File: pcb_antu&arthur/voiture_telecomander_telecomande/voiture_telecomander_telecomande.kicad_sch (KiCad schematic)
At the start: 31 parts, among them J1 batterie, J2 Ecran 7 segments, J3 bouton1, J4 bouton2, J5 interrupteur, J6 RGB, U1 ESP32-C6-DEVKITC-1-N8, U2 COM-09032

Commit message: changement de +5v à Alim_ESP
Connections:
- net +5V renamed Alim_ESP
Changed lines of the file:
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@@
+		)
+	)
+	(label "Alim_ESP"
+		(at 96.52 114.3 0)
+		(effects
+			(font
+				(size 1.27 1.27)
+			)
+			(justify left bottom)
 		)
 	)
@@
 		)
 	)
+	(label "Alim_ESP"
+		(at 55.88 114.3 180)
+		(effects
+			(font
+				(size 1.27 1.27)
+			)
+			(justify right bottom)
+		)
+	)
 	(label "DIO_ECRAN"
 		(at 55.88 88.9 180)
@@
 		)
 	)
+	(label "Alim_ESP"
+		(at 238.76 138.43 180)
+		(effects
+			(font
+				(size 1.27 1.27)
+			)
+			(justify right bottom)
+		)
+	)
 	(label "G"
 		(at 77.47 175.26 180)
@@
 	)
 	(symbol
-		(lib_id "power:+5V")
-		(at 238.76 138.43 90)
-		(unit 1)
-		(exclude_from_sim no)
-		(in_bom yes)
-		(on_board yes)
-		(dnp no)
-		(fields_autoplaced yes)
-		(property "Reference" "#PWR03"
-			(at 242.57 138.43 0)
-			(effects
-				(font
-					(size 1.27 1.27)
-				)
-				(hide yes)
-			)
-		)
-		(property "Value" "+5V"
-			(at 234.95 138.4299 90)
-			(effects
-				(font
-					(size 1.27 1.27)
-				)
-				(justify left)
-			)
-		)
-		(property "Footprint" ""
-			(at 238.76 138.43 0)
-			(effects
-				(font
-					(size 1.27 1.27)
-				)
-				(hide yes)
-			)
-		)
-		(property "Datasheet" ""
-			(at 238.76 138.43 0)
-			(effects
-				(font
-					(size 1.27 1.27)
-				)
-				(hide yes)
-			)
-		)
-		(property "Description" "Power symbol creates a global label with name \"+5V\""
-			(at 238.76 138.43 0)
-			(effects
-				(font
-					(size 1.27 1.27)
-				)
-				(hide yes)
-			)
-		)
-		(pin "1"
-		)
-		(instances
-			(project ""
-				(path "/570fb641-a88b-4e77-9989-d06242766e90"
-					(reference "#PWR03")
-					(unit 1)
-				)
-			)
-		)
-	)
-	(symbol
-		(lib_id "power:+5V")
-		(at 96.52 114.3 270)
-		(unit 1)
-		(exclude_from_sim no)
-		(in_bom yes)
-		(on_board yes)
-		(dnp no)
-		(fields_autoplaced yes)
-		(property "Reference" "#PWR09"
-			(at 92.71 114.3 0)
-			(effects
-				(font
-					(size 1.27 1.27)
-				)
-				(hide yes)
-			)
-		)
-		(property "Value" "+5V"
-			(at 100.33 114.2999 90)
-			(effects
-				(font
-					(size 1.27 1.27)
-				)
-				(justify left)
-			)
-		)
-		(property "Footprint" ""
-			(at 96.52 114.3 0)
-			(effects
-				(font
-					(size 1.27 1.27)
-				)
-				(hide yes)
-			)
-		)
-		(property "Datasheet" ""
-			(at 96.52 114.3 0)
-			(effects
-				(font
-					(size 1.27 1.27)
-				)
-				(hide yes)
-			)
-		)
-		(property "Description" "Power symbol creates a global label with name \"+5V\""
-			(at 96.52 114.3 0)
-			(effects
-				(font
-					(size 1.27 1.27)
-				)
-				(hide yes)
-			)
-		)
-		(pin "1"
-		)
-		(instances
-			(project ""
-				(path "/570fb641-a88b-4e77-9989-d06242766e90"
-					(reference "#PWR09")
-					(unit 1)
-				)
-			)
-		)
-	)
-	(symbol
 		(lib_id "power:GND")
 		(at 190.5 104.14 270)
@@
 					(unit 1)
 				)
-			)
-		)
-	)
-	(symbol
-		(lib_id "power:+5V")
-		(at 55.88 114.3 90)
-		(unit 1)
-		(exclude_from_sim no)
-		(in_bom yes)
-		(on_board yes)
-		(dnp no)
-		(fields_autoplaced yes)
-		(property "Reference" "#PWR08"
-			(at 59.69 114.3 0)
-			(effects
-				(font
-					(size 1.27 1.27)
-				)
-				(hide yes)
-			)
-		)
-		(property "Value" "+5V"
-			(at 52.07 114.2999 90)
-			(effects
-				(font
-					(size 1.27 1.27)
-				)
-				(justify left)
-			)
-		)
-		(property "Footprint" ""
-			(at 55.88 114.3 0)
-			(effects
-				(font
-					(size 1.27 1.27)
-				)
-				(hide yes)
-			)
-		)
-		(property "Datasheet" ""
-			(at 55.88 114.3 0)
-			(effects
-				(font
-					(size 1.27 1.27)
-				)
-				(hide yes)
-			)
-		)
-		(property "Description" "Power symbol creates a global label with name \"+5V\""
-			(at 55.88 114.3 0)
-			(effects
-				(font
-					(size 1.27 1.27)
-				)
-				(hide yes)
-			)
-		)
-		(pin "1"
-		)
-		(instances
-			(project ""
-				(path "/570fb641-a88b-4e77-9989-d06242766e90"
-					(reference "#PWR08")
-					(unit 1)
-				)

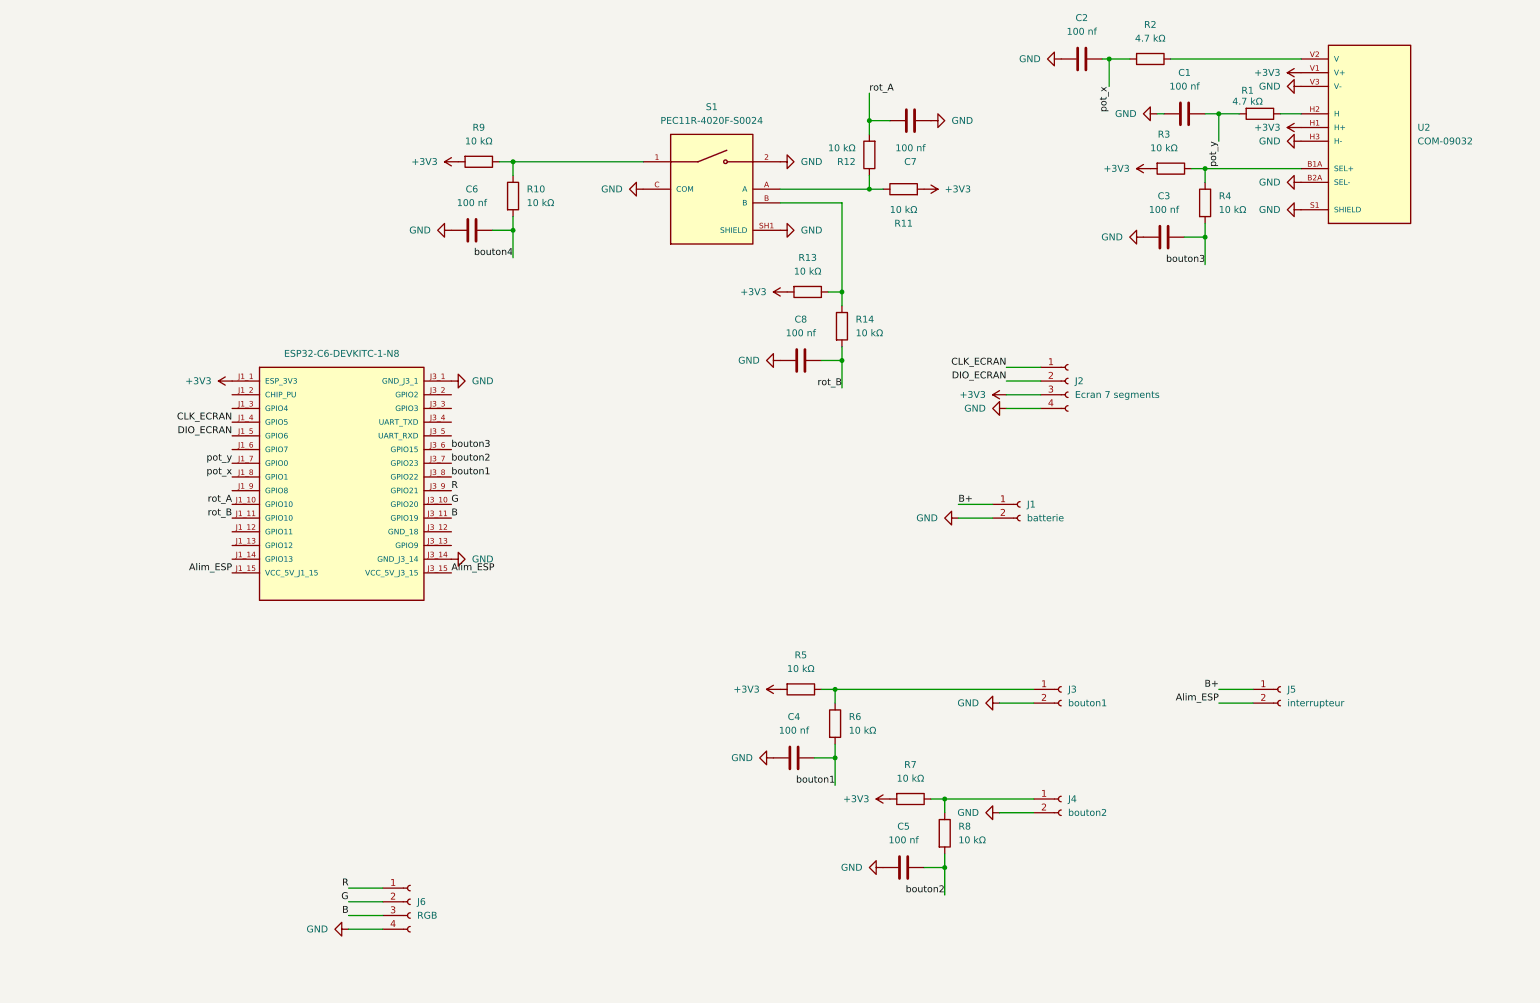
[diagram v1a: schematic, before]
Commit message: changement purement estetique dans le schema pour une meileur compréhension
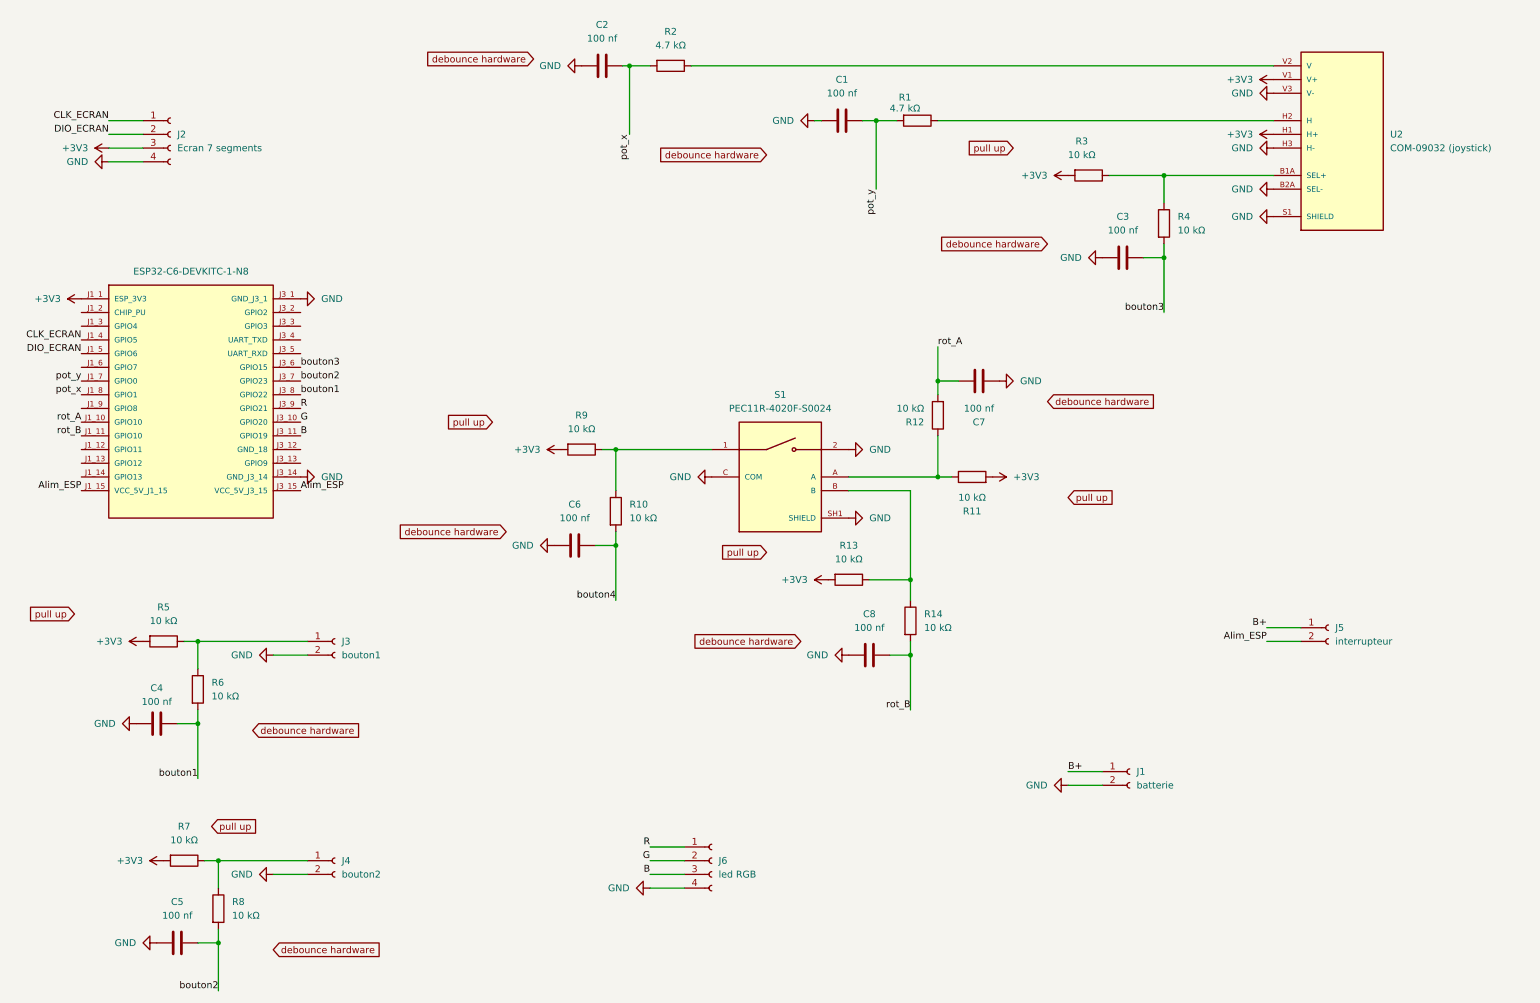
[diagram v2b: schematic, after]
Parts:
- J6: value RGB -> led RGB
- U2: value COM-09032 -> COM-09032 (joystick)
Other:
- moved on the sheet: C1, C2, C3, C4, C5, C6, C7, C8, J1, J2, J3, J4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

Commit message: mise a jour PCB antu_arthur
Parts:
- added J7: Conn_01x06_Socket, Connector_PinSocket_2.54mm:PinSocket_1x06_P2.54mm_Vertical, symbol Connector:Conn_01x06_Socket
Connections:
- net +3V3: now also J6.4 (Pin_4)
- net Alim_ESP: no longer J5.2 (Pin_2)
- net GND: now also J7.3 (Pin_3), J7.4 (Pin_4); no longer J6.4 (Pin_4)
- new net +5V: J7.5 (Pin_5), J7.6 (Pin_6)
- new net +BATT: J5.2 (Pin_2), J7.1 (Pin_1), J7.2 (Pin_2)

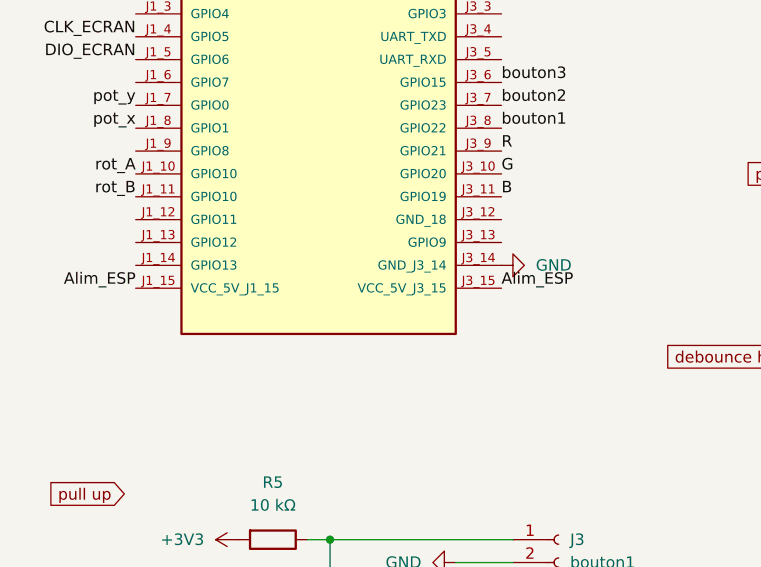
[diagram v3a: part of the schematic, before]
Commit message: ajout d'un converter buck
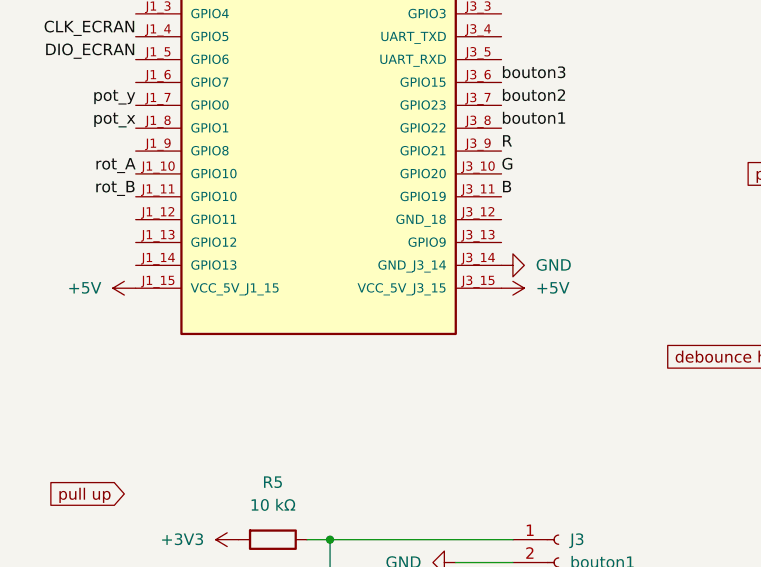
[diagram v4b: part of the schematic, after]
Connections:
- net Alim_ESP is gone; now on net +5V: U1.J1_15 (VCC_5V_J1_15), U1.J3_15 (VCC_5V_J3_15)
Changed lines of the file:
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@@
-		)
-	)
-	(label "Alim_ESP"
-		(at 68.58 99.06 0)
-		(effects
-			(font
-				(size 1.27 1.27)
-			)
-			(justify left bottom)
 		)
 	)
 	(label "R"
 		(at 133.35 165.1 180)
-		(effects
-			(font
-				(size 1.27 1.27)
-			)
-			(justify right bottom)
-		)
-	)
-	(label "Alim_ESP"
-		(at 27.94 99.06 180)
 		(effects
 			(font
@@
 	)
 	(symbol
+		(lib_id "power:+5V")
+		(at 68.58 99.06 270)
+		(unit 1)
+		(exclude_from_sim no)
+		(in_bom yes)
+		(on_board yes)
+		(dnp no)
+		(fields_autoplaced yes)
+		(property "Reference" "#PWR041"
+			(at 64.77 99.06 0)
+			(effects
+				(font
+					(size 1.27 1.27)
+				)
+				(hide yes)
+			)
+		)
+		(property "Value" "+5V"
+			(at 72.39 99.0599 90)
+			(effects
+				(font
+					(size 1.27 1.27)
+				)
+				(justify left)
+			)
+		)
+		(property "Footprint" ""
+			(at 68.58 99.06 0)
+			(effects
+				(font
+					(size 1.27 1.27)
+				)
+				(hide yes)
+			)
+		)
+		(property "Datasheet" ""
+			(at 68.58 99.06 0)
+			(effects
+				(font
+					(size 1.27 1.27)
+				)
+				(hide yes)
+			)
+		)
+		(property "Description" "Power symbol creates a global label with name \"+5V\""
+			(at 68.58 99.06 0)
+			(effects
+				(font
+					(size 1.27 1.27)
+				)
+				(hide yes)
+			)
+		)
+		(pin "1"
+		)
+		(instances
+			(project ""
+				(path "/570fb641-a88b-4e77-9989-d06242766e90"
+					(reference "#PWR041")
+					(unit 1)
+				)
+			)
+		)
+	)
+	(symbol
 		(lib_id "Device:R")
 		(at 46.99 167.64 270)
@@
 					(unit 1)
 				)
+			)
+		)
+	)
+	(symbol
+		(lib_id "power:+5V")
+		(at 27.94 99.06 90)
+		(unit 1)
+		(exclude_from_sim no)
+		(in_bom yes)
+		(on_board yes)
+		(dnp no)
+		(fields_autoplaced yes)
+		(property "Reference" "#PWR040"
+			(at 31.75 99.06 0)
+			(effects
+				(font
+					(size 1.27 1.27)
+				)
+				(hide yes)
+			)
+		)
+		(property "Value" "+5V"
+			(at 24.13 99.0599 90)
+			(effects
+				(font
+					(size 1.27 1.27)
+				)
+				(justify left)
+			)
+		)
+		(property "Footprint" ""
+			(at 27.94 99.06 0)
+			(effects
+				(font
+					(size 1.27 1.27)
+				)
+				(hide yes)
+			)
+		)
+		(property "Datasheet" ""
+			(at 27.94 99.06 0)
+			(effects
+				(font
+					(size 1.27 1.27)
+				)
+				(hide yes)
+			)
+		)
+		(property "Description" "Power symbol creates a global label with name \"+5V\""
+			(at 27.94 99.06 0)
+			(effects
+				(font
+					(size 1.27 1.27)
+				)
+				(hide yes)
+			)
+		)
+		(pin "1"
+		)
+		(instances
+			(project ""
+				(path "/570fb641-a88b-4e77-9989-d06242766e90"
+					(reference "#PWR040")
+					(unit 1)
+				)
